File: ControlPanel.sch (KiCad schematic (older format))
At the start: 0 parts

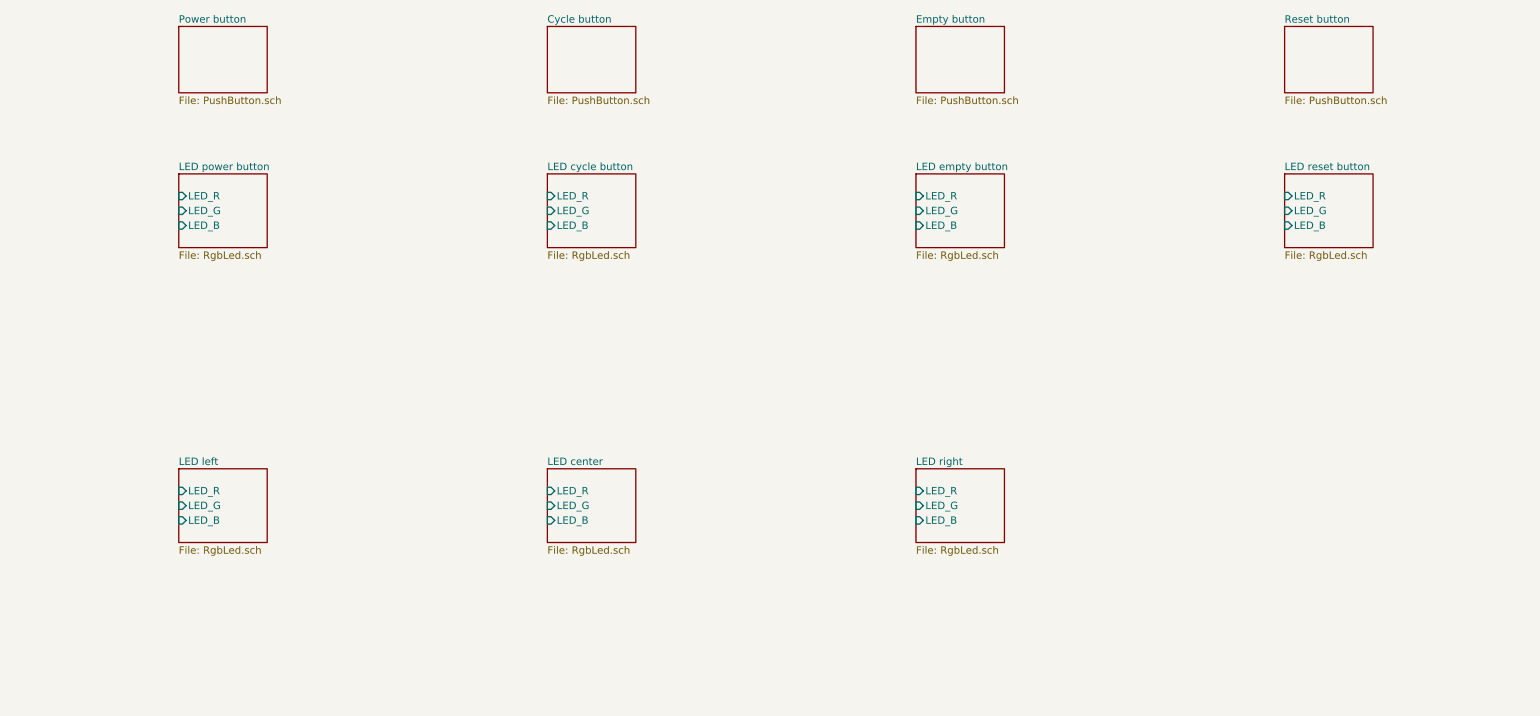
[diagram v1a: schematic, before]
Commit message: Add the push buttons and mounting holes
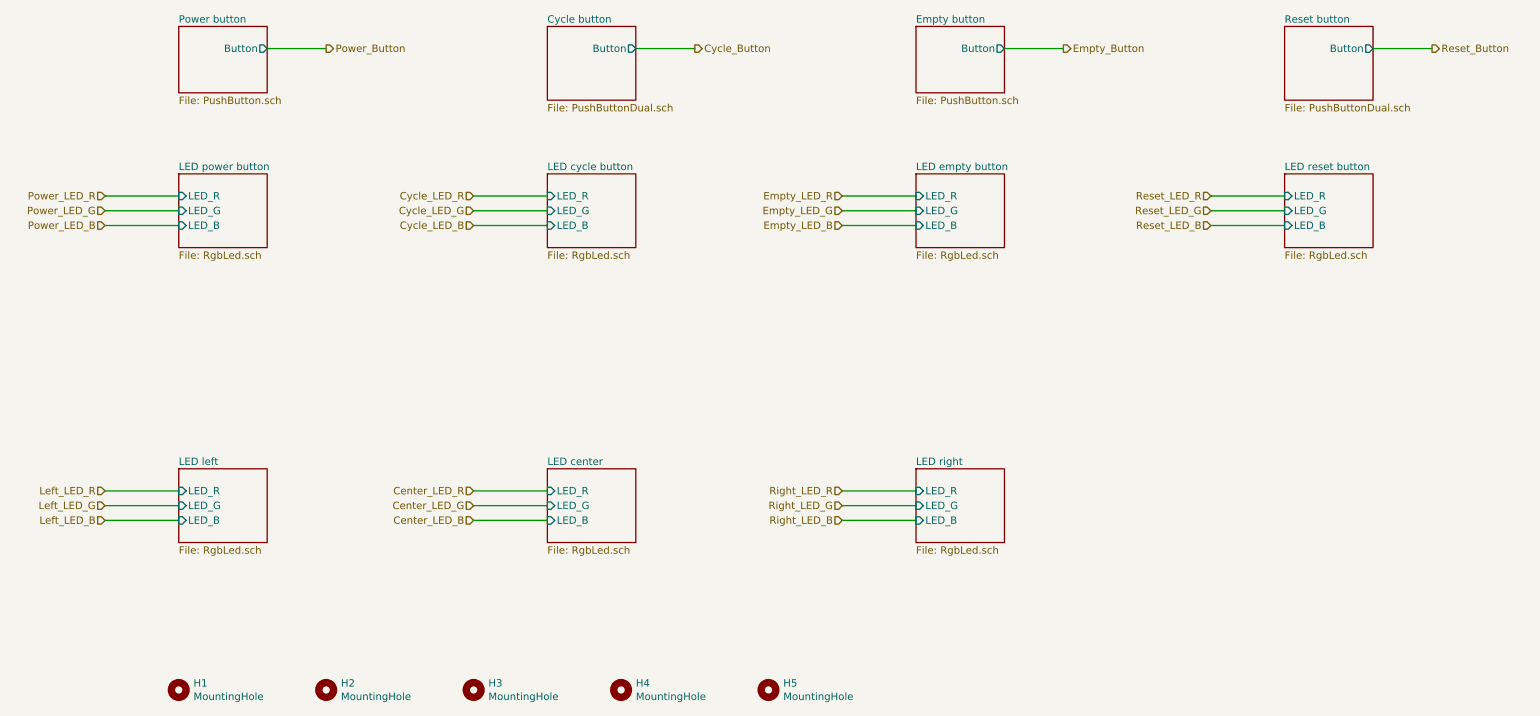
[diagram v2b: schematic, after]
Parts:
- added H1, H2, H3, H4, H5: MountingHole, MountingHole:MountingHole_4mm, symbol Mechanical:MountingHole
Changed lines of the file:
@@
+$EndSheet
+$Sheet
+S 7000 1500 600  450
+U 603C0699
+F0 "Empty button" 50
+F1 "PushButton.sch" 50
+F2 "Button" O R 7600 1650 50
+$EndSheet
+$Sheet
+S 2000 1500 600  450
+U 603C09F0
+F0 "Power button" 50
+F1 "PushButton.sch" 50
+F2 "Button" O R 2600 1650 50
+$EndSheet
+$Comp
+L Mechanical:MountingHole H1
+U 1 1 604CD5B9
+P 2000 6000
+F 0 "H1" H 2100 6046 50  0000 L CNN
+F 1 "MountingHole" H 2100 5955 50  0000 L CNN
+F 2 "MountingHole:MountingHole_4mm" H 2000 6000 50  0001 C CNN
+F 3 "~" H 2000 6000 50  0001 C CNN
+	1    2000 6000
+	1    0    0    -1
+$EndComp
+$Comp
+L Mechanical:MountingHole H2
+U 1 1 604CE3AC
+P 3000 6000
+F 0 "H2" H 3100 6046 50  0000 L CNN
+F 1 "MountingHole" H 3100 5955 50  0000 L CNN
+F 2 "MountingHole:MountingHole_4mm" H 3000 6000 50  0001 C CNN
+F 3 "~" H 3000 6000 50  0001 C CNN
+	1    3000 6000
+	1    0    0    -1
+$EndComp
+$Comp
+L Mechanical:MountingHole H3
+U 1 1 604CE505
+P 4000 6000
+F 0 "H3" H 4100 6046 50  0000 L CNN
+F 1 "MountingHole" H 4100 5955 50  0000 L CNN
+F 2 "MountingHole:MountingHole_4mm" H 4000 6000 50  0001 C CNN
+F 3 "~" H 4000 6000 50  0001 C CNN
+	1    4000 6000
+	1    0    0    -1
+$EndComp
+$Comp
+L Mechanical:MountingHole H4
+U 1 1 604CE803
+P 5000 6000
+F 0 "H4" H 5100 6046 50  0000 L CNN
+F 1 "MountingHole" H 5100 5955 50  0000 L CNN
+F 2 "MountingHole:MountingHole_4mm" H 5000 6000 50  0001 C CNN
+F 3 "~" H 5000 6000 50  0001 C CNN
+	1    5000 6000
+	1    0    0    -1
+$EndComp
+$Comp
+L Mechanical:MountingHole H5
+U 1 1 604CEBC5
+P 6000 6000
+F 0 "H5" H 6100 6046 50  0000 L CNN
+F 1 "MountingHole" H 6100 5955 50  0000 L CNN
+F 2 "MountingHole:MountingHole_4mm" H 6000 6000 50  0001 C CNN
+F 3 "~" H 6000 6000 50  0001 C CNN
+	1    6000 6000
+	1    0    0    -1
+$EndComp
+Text HLabel 3000 1650 2    50   Output ~ 0
+Power_Button
+Wire Wire Line
+	3000 1650 2600 1650
+Text HLabel 5500 1650 2    50   Output ~ 0
+Cycle_Button
+Wire Wire Line
+	5500 1650 5100 1650
+Text HLabel 8000 1650 2    50   Output ~ 0
+Empty_Button
+Wire Wire Line
+	8000 1650 7600 1650
+Text HLabel 10500 1650 2    50   Output ~ 0
+Reset_Button
+Wire Wire Line
+	10500 1650 10100 1650
+Text HLabel 1500 2650 0    50   Input ~ 0
+Power_LED_R
+Text HLabel 1500 2750 0    50   Input ~ 0
+Power_LED_G
+Text HLabel 1500 2850 0    50   Input ~ 0
+Power_LED_B
+Wire Wire Line
+	1500 2650 2000 2650
+Wire Wire Line
+	1500 2750 2000 2750
+Wire Wire Line
+	1500 2850 2000 2850
+Text HLabel 4000 2650 0    50   Input ~ 0
+Cycle_LED_R
+Text HLabel 4000 2750 0    50   Input ~ 0
+Cycle_LED_G
+Text HLabel 4000 2850 0    50   Input ~ 0
+Cycle_LED_B
+Wire Wire Line
+	4000 2650 4500 2650
+Wire Wire Line
+	4000 2750 4500 2750
+Wire Wire Line
+	4000 2850 4500 2850
+Text HLabel 6500 2650 0    50   Input ~ 0
+Empty_LED_R
+Text HLabel 6500 2750 0    50   Input ~ 0
+Empty_LED_G
+Text HLabel 6500 2850 0    50   Input ~ 0
+Empty_LED_B
+Wire Wire Line
+	6500 2650 7000 2650
+Wire Wire Line
+	6500 2750 7000 2750
+Wire Wire Line
+	6500 2850 7000 2850
+Text HLabel 9000 2650 0    50   Input ~ 0
+Reset_LED_R
+Text HLabel 9000 2750 0    50   Input ~ 0
+Reset_LED_G
+Text HLabel 9000 2850 0    50   Input ~ 0
+Reset_LED_B
+Wire Wire Line
+	9000 2650 9500 2650
+Wire Wire Line
+	9000 2750 9500 2750
+Wire Wire Line
+	9000 2850 9500 2850
+Text HLabel 1500 4650 0    50   Input ~ 0
+Left_LED_R
+Text HLabel 1500 4750 0    50   Input ~ 0
+Left_LED_G
+Text HLabel 1500 4850 0    50   Input ~ 0
+Left_LED_B
+Wire Wire Line
+	1500 4650 2000 4650
+Wire Wire Line
+	1500 4750 2000 4750
+Wire Wire Line
+	1500 4850 2000 4850
+Text HLabel 4000 4650 0    50   Input ~ 0
+Center_LED_R
+Text HLabel 4000 4750 0    50   Input ~ 0
+Center_LED_G
+Text HLabel 4000 4850 0    50   Input ~ 0
+Center_LED_B
+Wire Wire Line
+	4000 4650 4500 4650
+Wire Wire Line
+	4000 4750 4500 4750
+Wire Wire Line
+	4000 4850 4500 4850
+Text HLabel 6500 4650 0    50   Input ~ 0
+Right_LED_R
+Text HLabel 6500 4750 0    50   Input ~ 0
+Right_LED_G
+Text HLabel 6500 4850 0    50   Input ~ 0
+Right_LED_B
+Wire Wire Line
+	6500 4650 7000 4650
+Wire Wire Line
+	6500 4750 7000 4750
+Wire Wire Line
+	6500 4850 7000 4850
+$Sheet
+S 4500 1500 600  500
+U 604DE92D
+F0 "Cycle button" 50
+F1 "PushButtonDual.sch" 50
+F2 "Button" O R 5100 1650 50
 $EndSheet
 $Sheet
@@
 $EndSheet
 $Sheet
-S 4500 1500 600  450
-U 603C05C6
-F0 "Cycle button" 50
-F1 "PushButton.sch" 50
-$EndSheet
-$Sheet
-S 7000 1500 600  450
-U 603C0699
-F0 "Empty button" 50
-F1 "PushButton.sch" 50
-$EndSheet
-$Sheet
-S 9500 1500 600  450
-U 603C06CF
+S 9500 1500 600  500
+U 604E2A9A
 F0 "Reset button" 50
-F1 "PushButton.sch" 50
-$EndSheet
-$Sheet
-S 2000 1500 600  450
-U 603C09F0
-F0 "Power button" 50
-F1 "PushButton.sch" 50
+F1 "PushButtonDual.sch" 50
+F2 "Button" O R 10100 1650 50
 $EndSheet
 $EndSCHEMATC

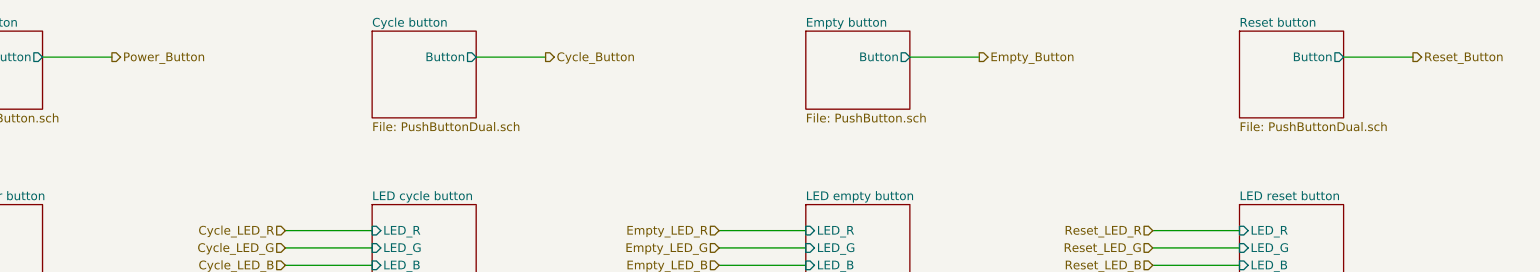
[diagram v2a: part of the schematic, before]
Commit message: Add fuse and more inter-page signals
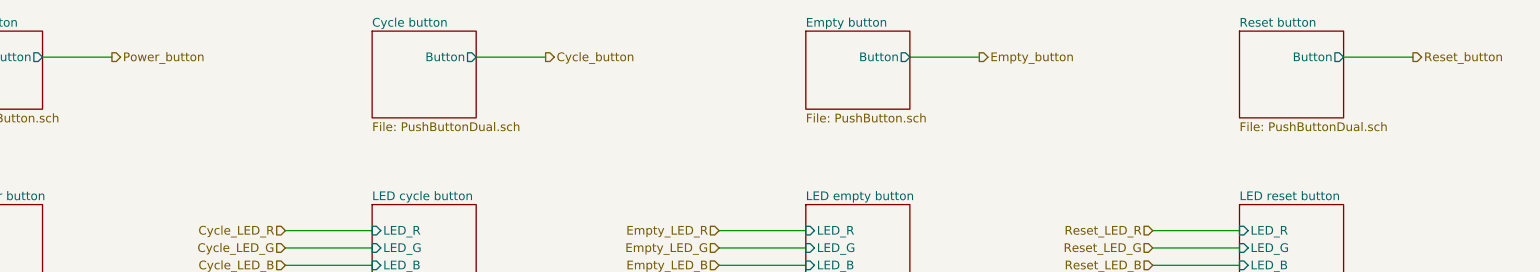
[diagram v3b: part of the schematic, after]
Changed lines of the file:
@@
 $EndComp
 Text HLabel 3000 1650 2    50   Output ~ 0
-Power_Button
+Power_button
 Wire Wire Line
 	3000 1650 2600 1650
 Text HLabel 5500 1650 2    50   Output ~ 0
-Cycle_Button
+Cycle_button
 Wire Wire Line
 	5500 1650 5100 1650
 Text HLabel 8000 1650 2    50   Output ~ 0
-Empty_Button
+Empty_button
 Wire Wire Line
 	8000 1650 7600 1650
 Text HLabel 10500 1650 2    50   Output ~ 0
-Reset_Button
+Reset_button
 Wire Wire Line
 	10500 1650 10100 1650
